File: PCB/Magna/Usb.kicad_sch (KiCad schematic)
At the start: 39 parts, among them J801 USB_A, J802 USB_C_Receptacle_USB2.0, J803 USB_B, U801 SRV05-4, U802 USB3300-EZK

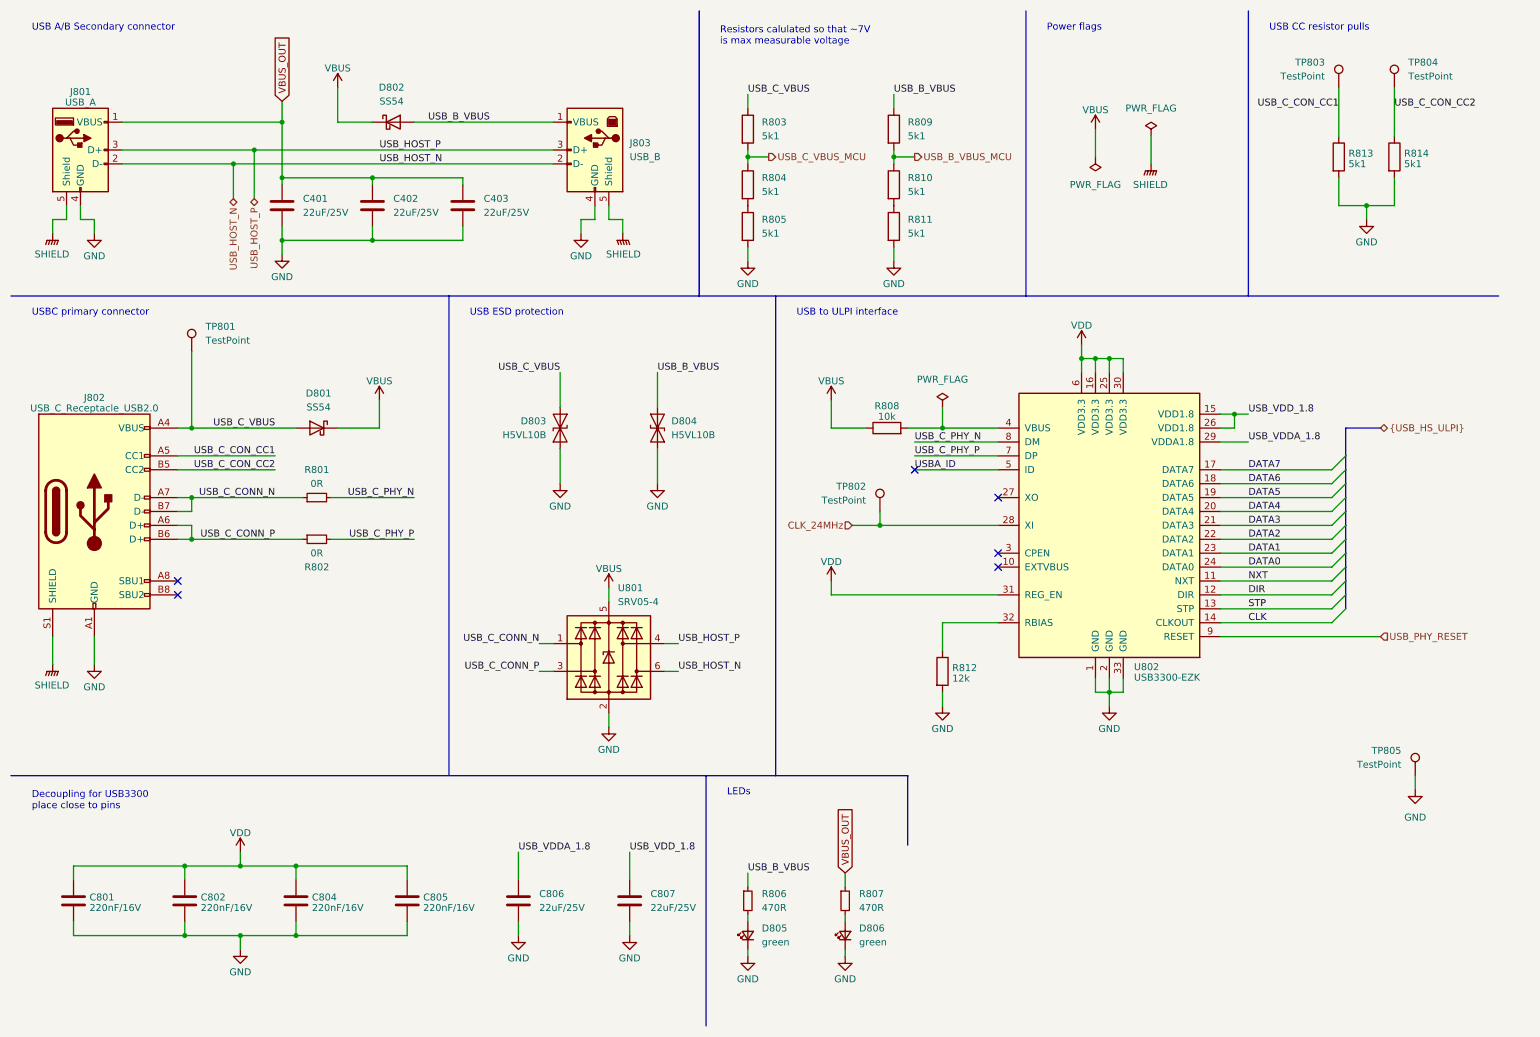
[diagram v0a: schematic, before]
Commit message: Mainboard layout (#19)
Also adds mounting holes to IO daughterboard
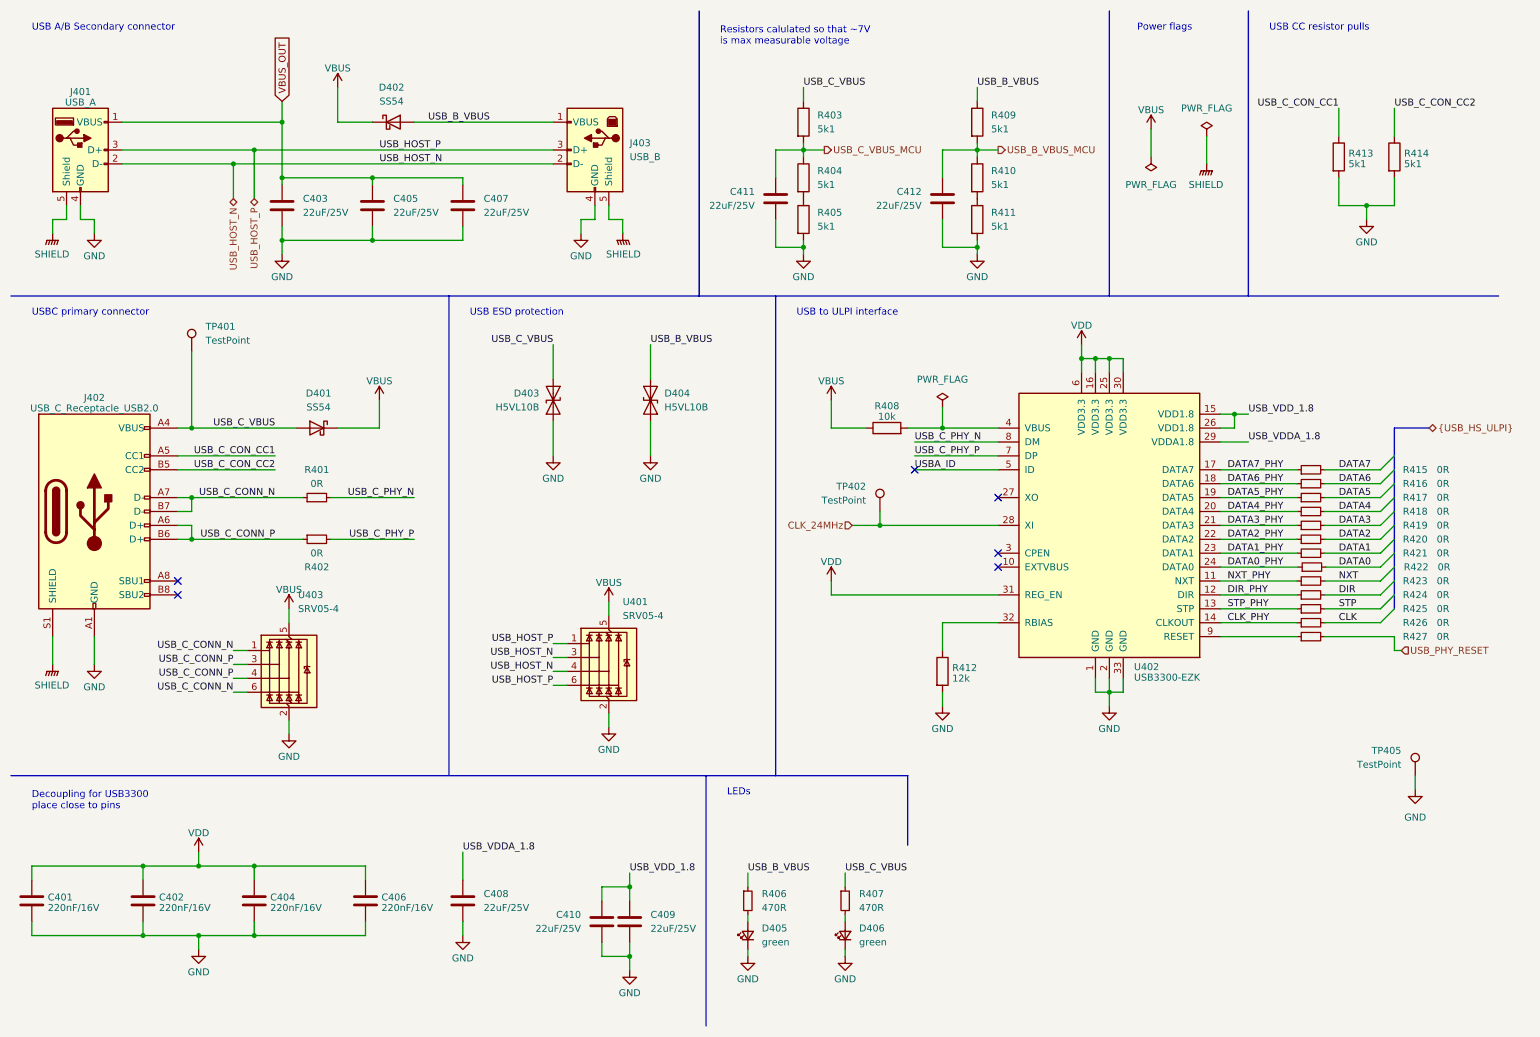
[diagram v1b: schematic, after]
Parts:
- removed TP803, TP804: TestPoint, TestPoint:TestPoint_Keystone_5000-5004_Miniature, symbol Connector:TestPoint
- added C410, C411, C412: 22uF/25V, Capacitor_SMD:C_0805_2012Metric_Pad1.18x1.45mm_HandSolder, symbol Device:C
- added R415, R416, R417, R418, R419, R420, R421, R422, R423, R424, R425, R426, R427: 0R, Resistor_SMD:R_0805_2012Metric_Pad1.20x1.40mm_HandSolder, symbol Device:R_Small
- added U403: SRV05-4, Package_TO_SOT_SMD:SOT-23-6, symbol Power_Protection:USBLC6-4SC6
- renumbered C801 to C401, C802 to C402, C401 to C403, C804 to C404, C402 to C405, C805 to C406, C403 to C407, C806 to C408, C807 to C409, D801 to D401, D802 to D402, D803 to D403, D804 to D404, D805 to D405, D806 to D406, J801 to J401, J802 to J402, J803 to J403, R801 to R401, R802 to R402, R803 to R403, R804 to R404, R805 to R405, R806 to R406, R807 to R407, R808 to R408, R809 to R409, R810 to R410, R811 to R411, R812 to R412, R813 to R413, R814 to R414, TP801 to TP401, TP802 to TP402, TP805 to TP405, U801 to U401, U802 to U402
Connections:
- net CLK: now also R426.2; no longer U402.14 (CLKOUT)
- net DATA0: now also R422.2; no longer U402.24 (DATA0)
- net DATA1: now also R421.2; no longer U402.23 (DATA1)
- net DATA2: now also R420.2; no longer U402.22 (DATA2)
- net DATA3: now also R419.2; no longer U402.21 (DATA3)
- net DATA4: now also R418.2; no longer U402.20 (DATA4)
- net DATA5: now also R417.2; no longer U402.19 (DATA5)
- net DATA6: now also R416.2; no longer U402.18 (DATA6)
- net DATA7: now also R415.2; no longer U402.17 (DATA7)
- net DIR: now also R424.2; no longer U402.12 (DIR)
- net GND: now also C410.2, C411.2, C412.2, U403.2 (GND)
- net NXT: now also R423.2; no longer U402.11 (NXT)
- net STP: now also R425.2; no longer U402.13 (STP)
- net USB_B_VBUS_MCU: now also C412.1
- net USB_C_CONN_N: now also U403.1 (I/O1), U403.6 (I/O4); no longer U401.1 (I/O1)
- net USB_C_CONN_P: now also U403.3 (I/O2), U403.4 (I/O3); no longer U401.3 (I/O2)
- net USB_C_VBUS: now also R407.1
- net USB_C_VBUS_MCU: now also C411.1
- net USB_HOST_N: now also U401.3 (I/O2), U401.4 (I/O3); no longer U401.6 (I/O4)
- net USB_HOST_P: now also U401.1 (I/O1), U401.6 (I/O4); no longer U401.4 (I/O3)
- net USB_PHY_RESET: now also R427.2; no longer U402.9 (RESET)
- net USB_VDD_1.8: now also C410.1
- net VBUS: now also U403.5 (VBUS)
- net VBUS_OUT: no longer R407.1
- new net: R427.1, U402.9 (RESET)
- new net CLK_PHY: R426.1, U402.14 (CLKOUT)
- new net DATA0_PHY: R422.1, U402.24 (DATA0)
- new net DATA1_PHY: R421.1, U402.23 (DATA1)
- new net DATA2_PHY: R420.1, U402.22 (DATA2)
- new net DATA3_PHY: R419.1, U402.21 (DATA3)
- new net DATA4_PHY: R418.1, U402.20 (DATA4)
- new net DATA5_PHY: R417.1, U402.19 (DATA5)
- new net DATA6_PHY: R416.1, U402.18 (DATA6)
- new net DATA7_PHY: R415.1, U402.17 (DATA7)
- new net DIR_PHY: R424.1, U402.12 (DIR)
- new net NXT_PHY: R423.1, U402.11 (NXT)
- new net STP_PHY: R425.1, U402.13 (STP)
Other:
- moved on the sheet: C401, C402, C404, C406, C408, C409, D403, D404, R403, R404, R405, R409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

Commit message: Update some files to KiCad8 and make ready for production
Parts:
- D403, D404: value H5VL10B -> H5VL10B

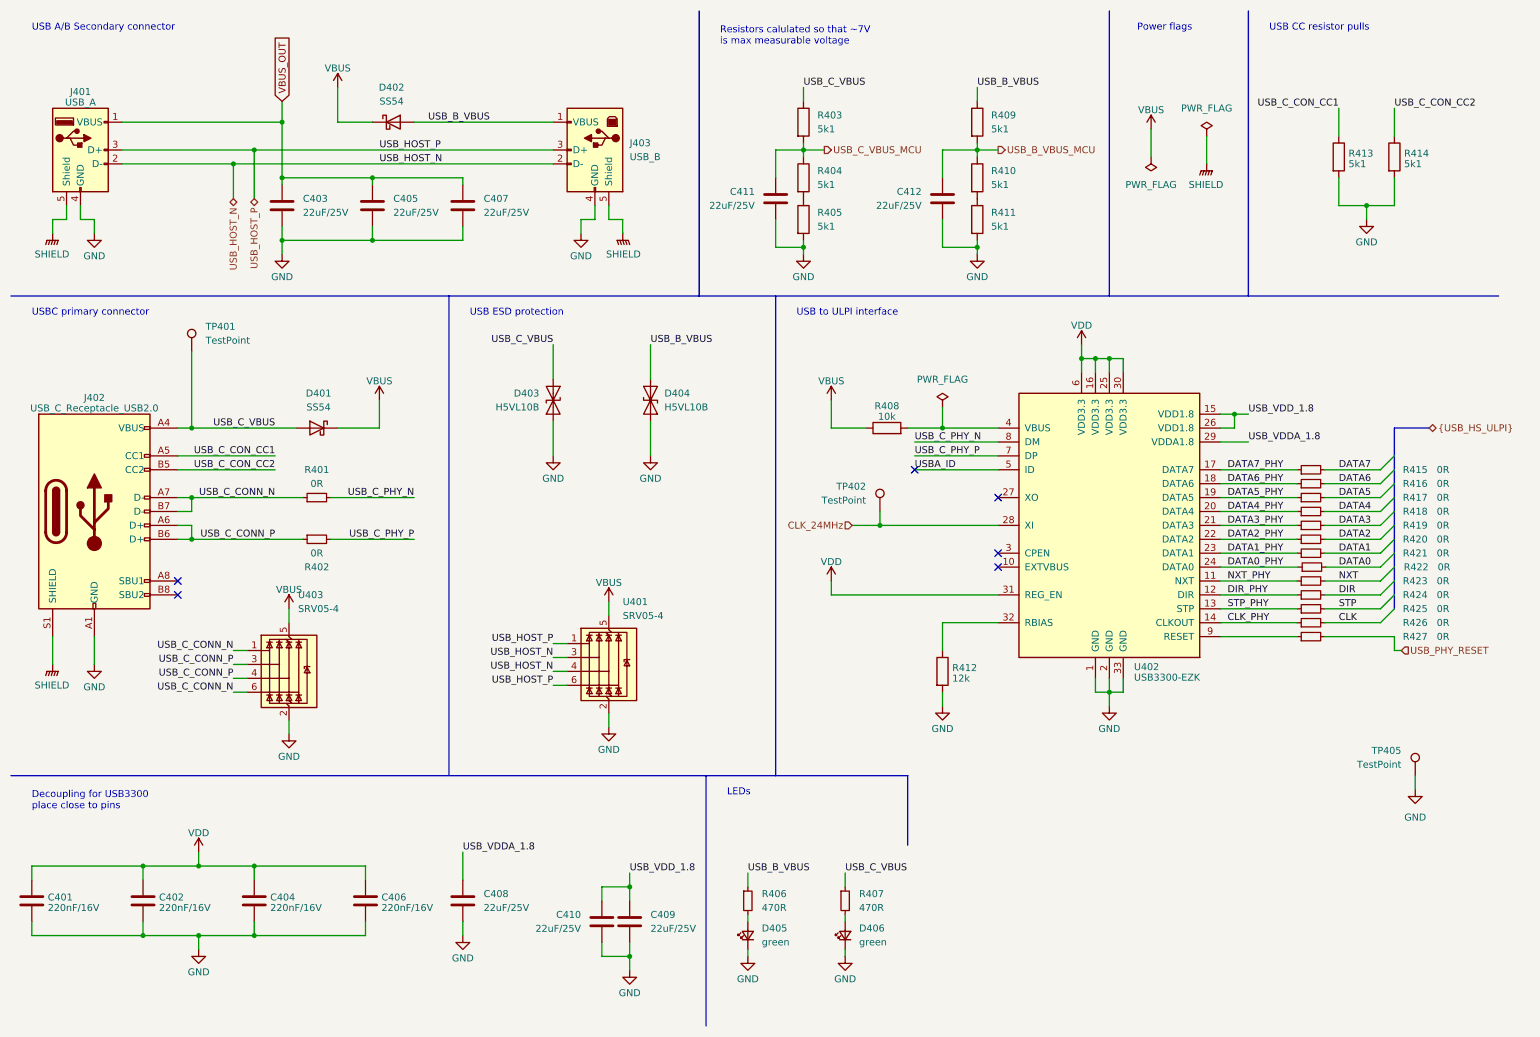
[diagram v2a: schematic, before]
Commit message: Update Project to Kicad 8.0 and prepare for production
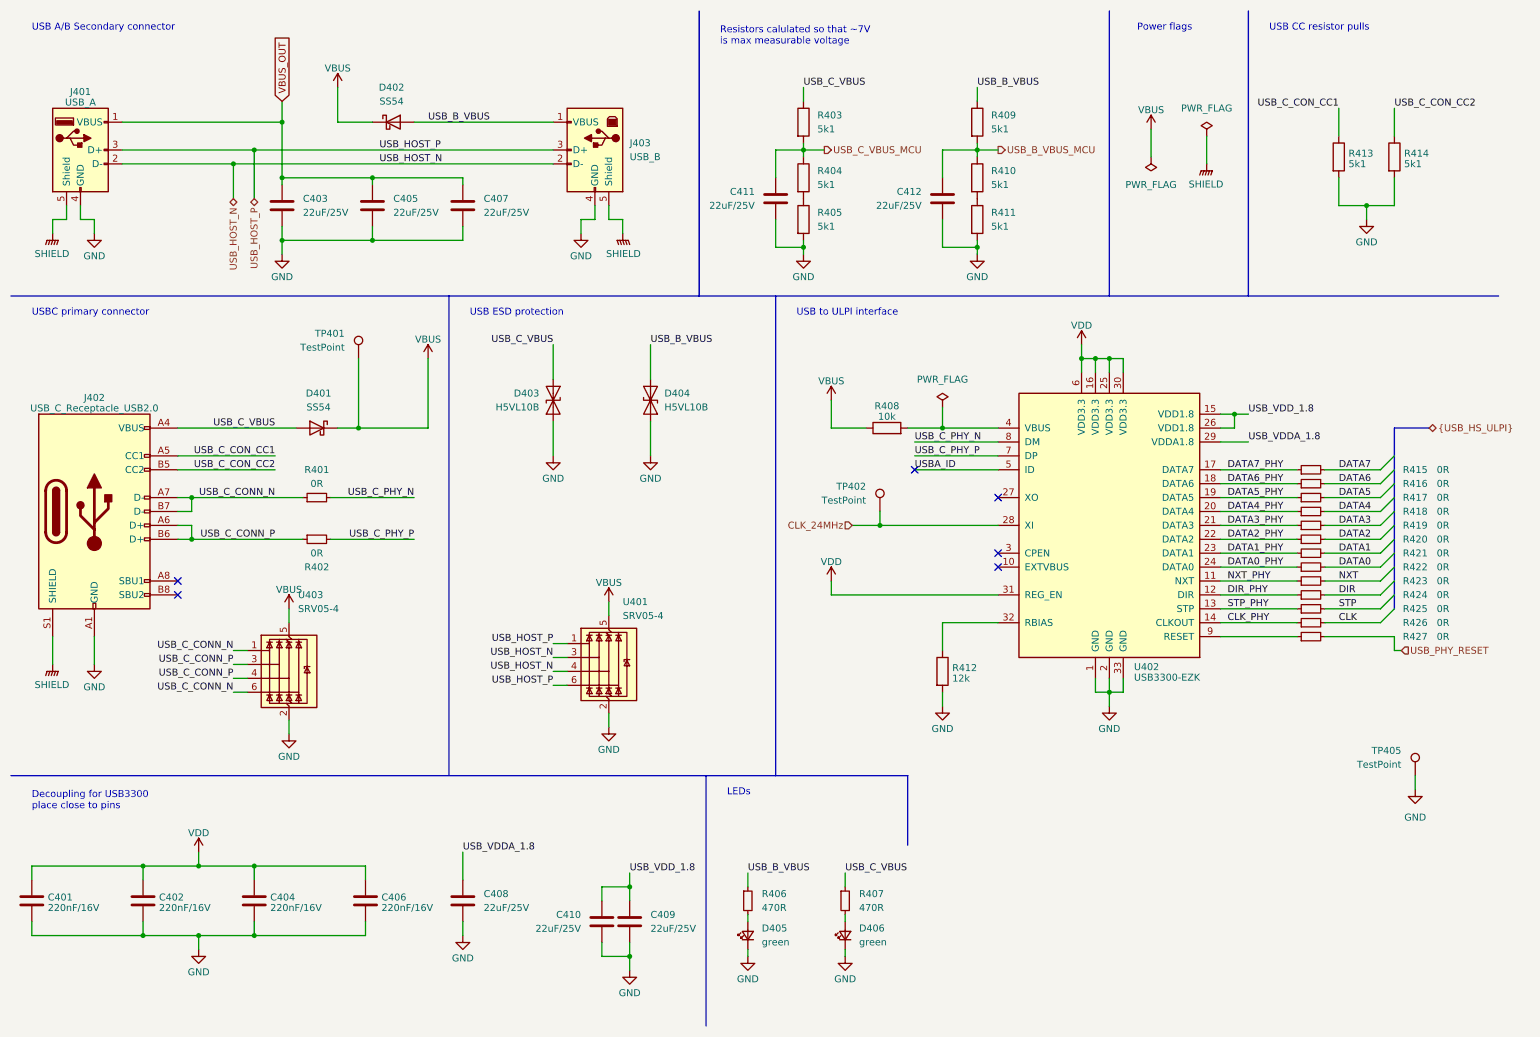
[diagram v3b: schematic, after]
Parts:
- D403, D404: footprint LED_SMD:LED_0402_1005Metric_Pad0.77x0.64mm_HandSolder -> Diode_SMD:D_0402_1005Metric
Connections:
- net USB_C_VBUS: no longer TP401.1
- net VBUS: now also TP401.1
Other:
- moved on the sheet: TP401

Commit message: Some updates to PCB
Honestly I cannot remember whats changed
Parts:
- J401: LCSC C293351 -> C456018
- J403: LCSC C114097 -> C720549
- R403, R404, R405, R409, R410, R411, R413, R414: LCSC C218638 -> C27834
- R406, R407: LCSC C706320 -> C17710
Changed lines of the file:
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@@
 			)
 		)
-		(property "LCSC" "C706320"
+		(property "LCSC" "C17710"
 			(at 147.32 175.26 0)
 			(effects
@@
 			)
 		)
-		(property "LCSC" "C218638"
+		(property "LCSC" "C27834"
 			(at 265.43 39.37 0)
 			(effects
@@
 			)
 		)
-		(property "LCSC" "C218638"
+		(property "LCSC" "C27834"
 			(at 189.23 50.8 0)
 			(effects
@@
 			)
 		)
-		(property "LCSC" "C218638"
+		(property "LCSC" "C27834"
 			(at 157.48 43.18 0)
 			(effects
@@
 			)
 		)
-		(property "LCSC" "C218638"
+		(property "LCSC" "C27834"
 			(at 157.48 50.8 0)
 			(effects
@@
 			)
 		)
-		(property "LCSC" "C218638"
+		(property "LCSC" "C27834"
 			(at 255.27 39.37 0)
 			(effects
@@
 			)
 		)
-		(property "LCSC" "C218638"
+		(property "LCSC" "C27834"
 			(at 157.48 33.02 0)
 			(effects
@@
 			)
 		)
-		(property "LCSC" "C218638"
+		(property "LCSC" "C27834"
 			(at 189.23 33.02 0)
 			(effects
@@
 			)
 		)
-		(property "LCSC" "C293351"
-			(at 25.4 38.1 0)
-			(effects
-				(font
-					(size 1.27 1.27)
-				)
-				(hide yes)
-			)
-		)
-		(property "LSCS" ""
+		(property "LCSC" "C456018"
 			(at 25.4 38.1 0)
 			(effects
@@
 			)
 		)
-		(property "LCSC" "C706320"
+		(property "LCSC" "C17710"
 			(at 165.1 175.26 0)
 			(effects
@@
 			)
 		)
-		(property "LCSC" "C218638"
+		(property "LCSC" "C27834"
 			(at 189.23 43.18 0)
 			(effects
@@
 			)
 		)
-		(property "LCSC" "C114097"
-			(at 119.38 38.1 0)
-			(effects
-				(font
-					(size 1.27 1.27)
-				)
-				(hide yes)
-			)
-		)
-		(property "LSCS" ""
+		(property "LCSC" "C720549"
 			(at 119.38 38.1 0)
 			(effects
